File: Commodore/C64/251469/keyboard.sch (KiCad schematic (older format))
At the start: 8 parts, among them CN1 Keyboard, U20 LM556, U8 7406

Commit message: .
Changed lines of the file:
@@
 encoding utf-8
 Sheet 9 15
-Title "Commodore 64 - Keyboard section (schematic #251469)"
+Title "Commodore 64 - Keyboard (schematic #251469)"
 Date "2019-07-21"
 Rev "0.1"
@@
 P 3400 2000
 F 0 "#PWR0211" H 3400 1750 50  0001 C CNN
-F 1 "GND" H 3405 1827 50  0000 C CNN
+F 1 "GND" H 3405 1827 50  0001 C CNN
 F 2 "" H 3400 2000 50  0001 C CNN
 F 3 "" H 3400 2000 50  0001 C CNN
@@
 P 650 1450
 F 0 "#PWR0212" H 650 1200 50  0001 C CNN
-F 1 "GND" H 650 1300 50  0000 C CNN
+F 1 "GND" H 650 1300 50  0001 C CNN
 F 2 "" H 650 1450 50  0001 C CNN
 F 3 "" H 650 1450 50  0001 C CNN

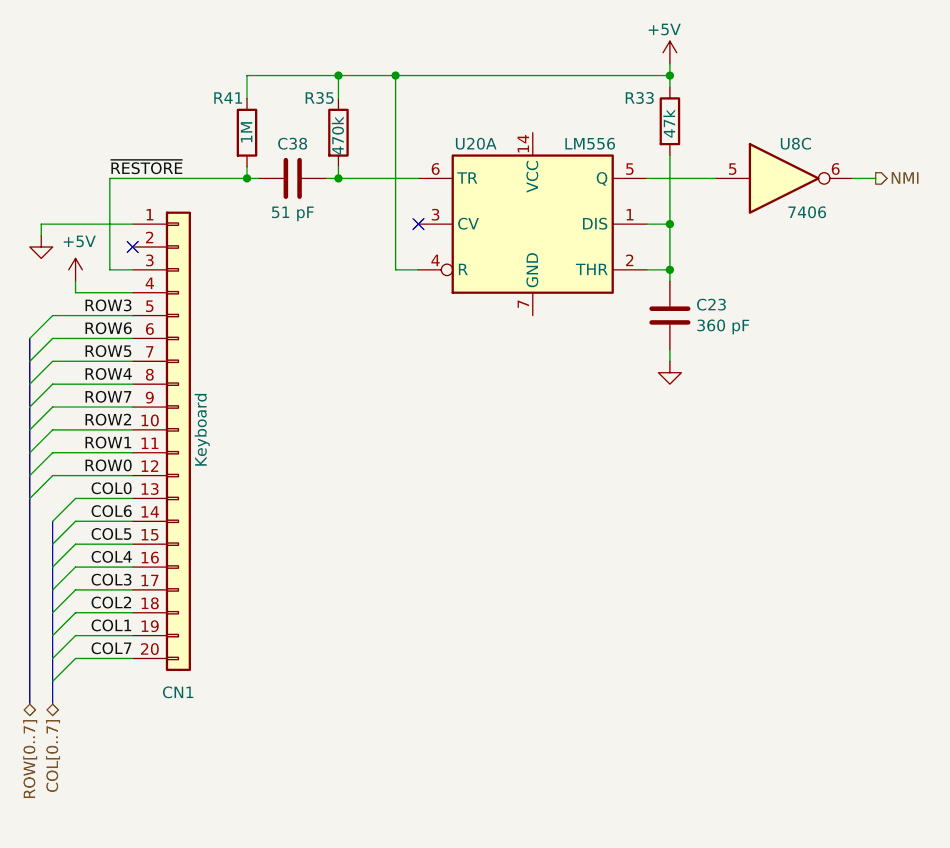
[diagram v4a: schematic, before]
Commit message: refac: extracted CPU to separate sheet
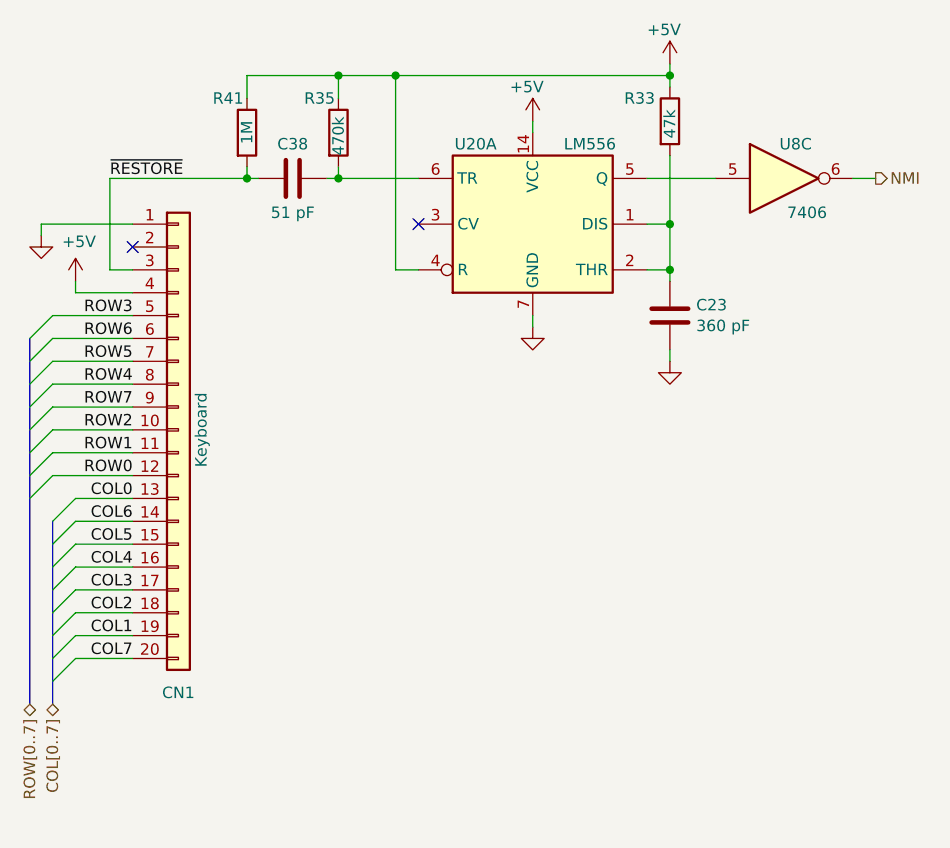
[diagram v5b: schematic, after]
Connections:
- net +5V: now also U20.14 (VCC)
- net GND: now also U20.7 (GND)
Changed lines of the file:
@@
 $Descr A4 11693 8268
 encoding utf-8
-Sheet 12 16
+Sheet 11 17
 Title "Commodore 64 - Keyboard (schematic #251469)"
 Date "2019-07-21"
@@
 Wire Wire Line
 	4200 1200 4300 1200
+$Comp
+L power:+5V #PWR?
+U 1 1 5D542ED2
+P 2800 950
+AR Path="/5D542ED2" Ref="#PWR?"  Part="1"
+AR Path="/5D28EBAC/5D542ED2" Ref="#PWR?"  Part="1"
+AR Path="/5D4AE438/5D542ED2" Ref="#PWR?"  Part="1"
+AR Path="/5D9CCECB/5D542ED2" Ref="#PWR?"  Part="1"
+AR Path="/5D943305/5D7052DF/5D542ED2" Ref="#PWR?"  Part="1"
+F 0 "#PWR?" H 2800 800 50  0001 C CNN
+F 1 "+5V" H 2700 1100 50  0000 L CNN
+F 2 "" H 2800 950 50  0001 C CNN
+F 3 "" H 2800 950 50  0001 C CNN
+	1    2800 950
+	1    0    0    -1
+$EndComp
+$Comp
+L power:GND #PWR?
+U 1 1 5D5434CB
+P 2800 1850
+F 0 "#PWR?" H 2800 1600 50  0001 C CNN
+F 1 "GND" H 2805 1677 50  0001 C CNN
+F 2 "" H 2800 1850 50  0001 C CNN
+F 3 "" H 2800 1850 50  0001 C CNN
+	1    2800 1850
+	1    0    0    -1
+$EndComp
+Wire Wire Line
+	2800 1850 2800 1800
+Wire Wire Line
+	2800 950  2800 1000
 Wire Bus Line
 	700  2700 700  3500

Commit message: Checked all board caps (except RF modulator) in BOM against Service Manual parts list, and added type, voltage ratings and tolerance information from parts list to them
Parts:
- C23: Type (none) -> Ceramic; Voltage Rating (none) -> 50V; Voltage Tolerance (none) -> 10%
- C38: Type (none) -> Ceramic; Voltage Rating (none) -> 50V; Voltage Tolerance (none) -> 5%
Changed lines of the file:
@@
 EESchema Schematic File Version 4
 LIBS:C64B-cache
-EELAYER 29 0
+EELAYER 30 0
 EELAYER END
 $Descr A4 11693 8268
@@
 F 2 "" H 1788 1050 50  0001 C CNN
 F 3 "~" H 1750 1200 50  0001 C CNN
+F 4 "Ceramic" H 1750 1200 50  0001 C CNN "Type"
+F 5 "50V" H 1750 1200 50  0001 C CNN "Voltage Rating"
+F 6 "5%" H 1750 1200 50  0001 C CNN "Voltage Tolerance"
 	1    1750 1200
 	0    1    1    0
@@
 F 2 "" H 3438 1650 50  0001 C CNN
 F 3 "~" H 3400 1800 50  0001 C CNN
+F 4 "Ceramic" H 3400 1800 50  0001 C CNN "Type"
+F 5 "50V" H 3400 1800 50  0001 C CNN "Voltage Rating"
+F 6 "10%" H 3400 1800 50  0001 C CNN "Voltage Tolerance"
 	1    3400 1800
 	1    0    0    -1
